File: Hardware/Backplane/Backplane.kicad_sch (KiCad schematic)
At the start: 9 parts, among them J1 10018784-10201TLF

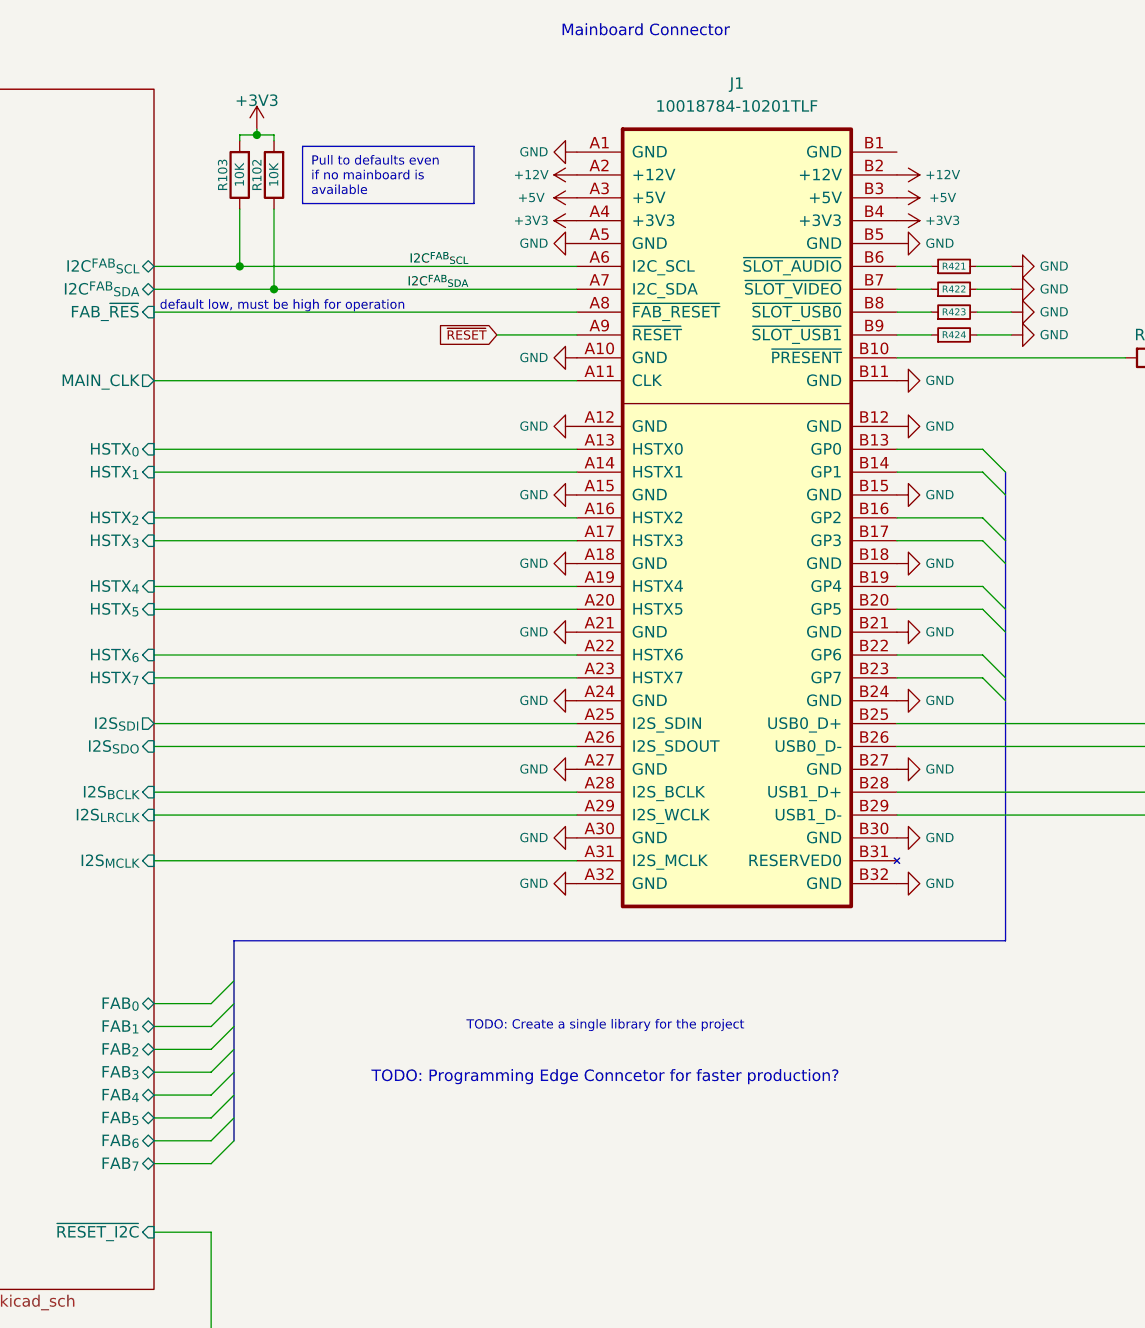
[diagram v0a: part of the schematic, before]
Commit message: Fixes several issues with the backplane schematic.
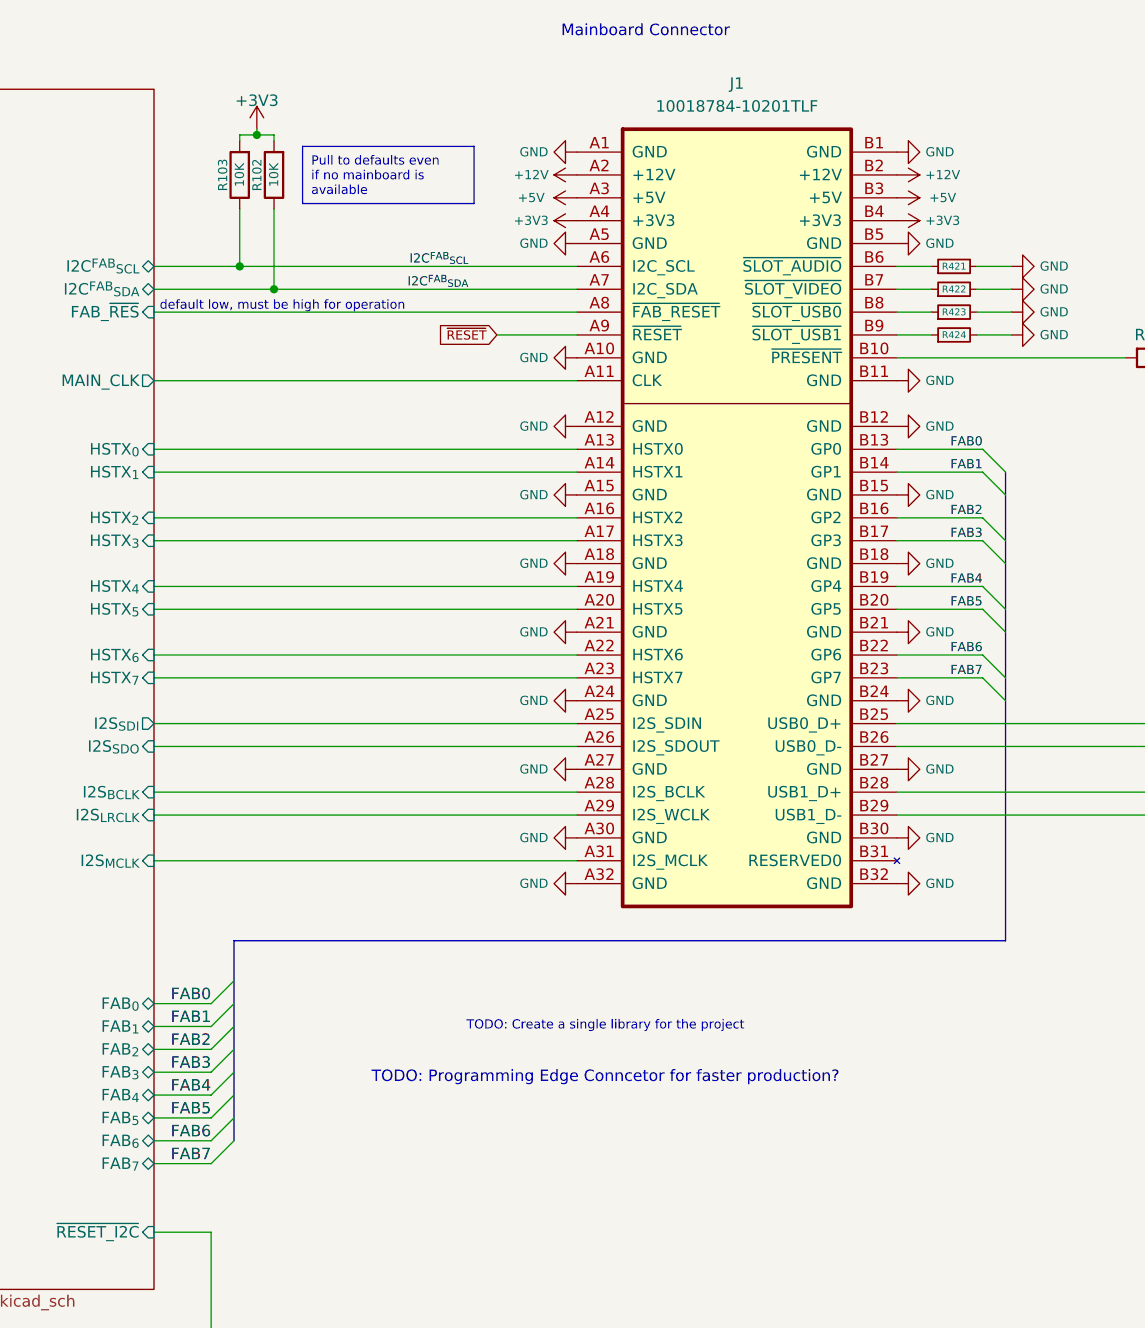
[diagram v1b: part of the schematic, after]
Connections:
- net GND: now also J1.B1 (GND)
- net FAB0: now reaches J1.B13 (GP0)
- net FAB1: now reaches J1.B14 (GP1)
- net FAB2: now reaches J1.B16 (GP2)
- net FAB3: now reaches J1.B17 (GP3)
- net FAB4: now reaches J1.B19 (GP4)
- net FAB5: now reaches J1.B20 (GP5)
- net FAB6: now reaches J1.B22 (GP6)
- net FAB7: now reaches J1.B23 (GP7)
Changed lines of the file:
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@@
+		)
+	)
+	(label "FAB4"
+		(at 82.55 137.16 180)
+		(effects
+			(font
+				(size 1.27 1.27)
+			)
+			(justify right bottom)
+		)
+	)
+	(label "FAB3"
+		(at 82.55 134.62 180)
+		(effects
+			(font
+				(size 1.27 1.27)
+			)
+			(justify right bottom)
 		)
 	)
@@
 		)
 	)
+	(label "FAB5"
+		(at 168.275 83.185 180)
+		(effects
+			(font
+				(size 1.016 1.016)
+			)
+			(justify right bottom)
+		)
+	)
+	(label "FAB1"
+		(at 168.275 67.945 180)
+		(effects
+			(font
+				(size 1.016 1.016)
+			)
+			(justify right bottom)
+		)
+	)
 	(label "USB_{1}_D+"
 		(at 221.615 111.76 0)
@@
 		)
 	)
+	(label "FAB3"
+		(at 168.275 75.565 180)
+		(effects
+			(font
+				(size 1.016 1.016)
+			)
+			(justify right bottom)
+		)
+	)
+	(label "FAB7"
+		(at 168.275 90.805 180)
+		(effects
+			(font
+				(size 1.016 1.016)
+			)
+			(justify right bottom)
+		)
+	)
+	(label "FAB0"
+		(at 168.275 65.405 180)
+		(effects
+			(font
+				(size 1.016 1.016)
+			)
+			(justify right bottom)
+		)
+	)
+	(label "FAB5"
+		(at 82.55 139.7 180)
+		(effects
+			(font
+				(size 1.27 1.27)
+			)
+			(justify right bottom)
+		)
+	)
+	(label "FAB2"
+		(at 82.55 132.08 180)
+		(effects
+			(font
+				(size 1.27 1.27)
+			)
+			(justify right bottom)
+		)
+	)
+	(label "FAB6"
+		(at 168.275 88.265 180)
+		(effects
+			(font
+				(size 1.016 1.016)
+			)
+			(justify right bottom)
+		)
+	)
+	(label "FAB0"
+		(at 82.55 127 180)
+		(effects
+			(font
+				(size 1.27 1.27)
+			)
+			(justify right bottom)
+		)
+	)
+	(label "FAB1"
+		(at 82.55 129.54 180)
+		(effects
+			(font
+				(size 1.27 1.27)
+			)
+			(justify right bottom)
+		)
+	)
+	(label "FAB2"
+		(at 168.275 73.025 180)
+		(effects
+			(font
+				(size 1.016 1.016)
+			)
+			(justify right bottom)
+		)
+	)
 	(label "USB_{0}_D-"
 		(at 221.615 98.425 0)
@@
 			)
 			(justify left bottom)
+		)
+	)
+	(label "FAB6"
+		(at 82.55 142.24 180)
+		(effects
+			(font
+				(size 1.27 1.27)
+			)
+			(justify right bottom)
+		)
+	)
+	(label "FAB4"
+		(at 168.275 80.645 180)
+		(effects
+			(font
+				(size 1.016 1.016)
+			)
+			(justify right bottom)
+		)
+	)
+	(label "FAB7"
+		(at 82.55 144.78 180)
+		(effects
+			(font
+				(size 1.27 1.27)
+			)
+			(justify right bottom)
 		)
 	)
@@
 					(unit 1)
 				)
+			)
+		)
+	)
+	(symbol
+		(lib_id "power:GND")
+		(at 158.75 32.385 90)
+		(mirror x)
+		(unit 1)
+		(body_style 1)
+		(exclude_from_sim no)
+		(in_bom yes)
+		(on_board yes)
+		(in_pos_files yes)
+		(dnp no)
+		(property "Reference" "#PWR01036"
+			(at 165.1 32.385 0)
+			(hide yes)
+			(show_name no)
+			(do_not_autoplace no)
+			(effects
+				(font
+					(size 1.016 1.016)
+				)
+			)
+		)
+		(property "Value" "GND"
+			(at 161.925 32.385 90)
+			(show_name no)
+			(do_not_autoplace no)
+			(effects
+				(font
+					(size 1.016 1.016)
+				)
+				(justify right)
+			)
+		)
+		(property "Footprint" ""
+			(at 158.75 32.385 0)
+			(hide yes)
+			(show_name no)
+			(do_not_autoplace no)
+			(effects
+				(font
+					(size 1.27 1.27)
+				)
+			)
+		)
+		(property "Datasheet" ""
+			(at 158.75 32.385 0)
+			(hide yes)
+			(show_name no)
+			(do_not_autoplace no)
+			(effects
+				(font
+					(size 1.27 1.27)
+				)
+			)
+		)
+		(property "Description" "Power symbol creates a global label with name \"GND\" , ground"
+			(at 158.75 32.385 0)
+			(hide yes)
+			(show_name no)
+			(do_not_autoplace no)
+			(effects
+				(font
+					(size 1.27 1.27)
+				)
+			)
+		)
+		(pin "1"
+		)
+		(instances
+			(project "Backplane"
+				(path "/c6da991a-d3ed-4ac1-8b0d-12cd7ba8539b"
+					(reference "#PWR01036")
+					(unit 1)
+				)

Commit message: Improves backplane schematic even more
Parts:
- added R441: 0, Resistor_SMD:R_0603_1608Metric, symbol Device:R_Small
- J1: symbol Home Computer:AHC-CONN-CPU -> Home Computer:AHC-CONN-CPU-HOST
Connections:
- net +3V3: now also R441.1
- net GND: no longer J1.A5 (GND)
- new net: J1.A5 (+3V3_ID), R441.2
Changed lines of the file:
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@@
 		(color 0 0 0 0)
 	)
+	(junction
+		(at 114.3 42.545)
+		(diameter 0)
+		(color 0 0 0 0)
+	)
 	(bus_entry
 		(at 82.55 137.16)
@@
 	(wire
 		(pts
+			(xy 113.665 42.545) (xy 114.3 42.545)
+		)
+		(stroke
+			(width 0)
+			(type default)
+		)
+	)
+	(wire
+		(pts
 			(xy 76.2 142.24) (xy 82.55 142.24)
 		)
@@
 	(wire
 		(pts
+			(xy 107.95 42.545) (xy 108.585 42.545)
+		)
+		(stroke
+			(width 0)
+			(type default)
+		)
+	)
+	(wire
+		(pts
 			(xy 76.2 152.4) (xy 82.55 152.4)
 		)
@@
 	(wire
 		(pts
+			(xy 114.3 42.545) (xy 123.19 42.545)
+		)
+		(stroke
+			(width 0)
+			(type default)
+		)
+	)
+	(wire
+		(pts
 			(xy 76.2 50.165) (xy 123.19 50.165)
 		)
@@
 	)
 	(symbol
-		(lib_id "Home Computer:AHC-CONN-CPU")
+		(lib_id "Home Computer:AHC-CONN-CPU-HOST")
 		(at 140.97 73.025 0)
 		(unit 1)
@@
 	)
 	(symbol
+		(lib_id "power:PWR_FLAG")
+		(at 114.3 42.545 0)
+		(unit 1)
+		(body_style 1)
+		(exclude_from_sim no)
+		(in_bom yes)
+		(on_board yes)
+		(in_pos_files yes)
+		(dnp no)
+		(fields_autoplaced yes)
+		(property "Reference" "#FLG0439"
+			(at 114.3 40.64 0)
+			(hide yes)
+			(show_name no)
+			(do_not_autoplace no)
+			(effects
+				(font
+					(size 1.016 1.016)
+				)
+			)
+		)
+		(property "Value" "PWR_FLAG"
+			(at 114.3 37.465 0)
+			(hide yes)
+			(show_name no)
+			(do_not_autoplace no)
+			(effects
+				(font
+					(size 1.016 1.016)
+				)
+			)
+		)
+		(property "Footprint" ""
+			(at 114.3 42.545 0)
+			(hide yes)
+			(show_name no)
+			(do_not_autoplace no)
+			(effects
+				(font
+					(size 1.27 1.27)
+				)
+			)
+		)
+		(property "Datasheet" ""
+			(at 114.3 42.545 0)
+			(hide yes)
+			(show_name no)
+			(do_not_autoplace no)
+			(effects
+				(font
+					(size 1.27 1.27)
+				)
+			)
+		)
+		(property "Description" "Special symbol for telling ERC where power comes from"
+			(at 114.3 42.545 0)
+			(hide yes)
+			(show_name no)
+			(do_not_autoplace no)
+			(effects
+				(font
+					(size 1.27 1.27)
+				)
+			)
+		)
+		(pin "1"
+		)
+		(instances
+			(project "Backplane"
+				(path "/c6da991a-d3ed-4ac1-8b0d-12cd7ba8539b"
+					(reference "#FLG0439")
+					(unit 1)
+				)
+			)
+		)
+	)
+	(symbol
 		(lib_id "power:GND")
 		(at 123.19 100.965 270)
@@
 	)
 	(symbol
+		(lib_id "power:+3V3")
+		(at 107.95 42.545 90)
+		(mirror x)
+		(unit 1)
+		(body_style 1)
+		(exclude_from_sim no)
+		(in_bom yes)
+		(on_board yes)
+		(in_pos_files yes)
+		(dnp no)
+		(property "Reference" "#PWR0133"
+			(at 111.76 42.545 0)
+			(hide yes)
+			(show_name no)
+			(do_not_autoplace no)
+			(effects
+				(font
+					(size 1.016 1.016)
+				)
+			)
+		)
+		(property "Value" "+3V3"
+			(at 102.87 42.545 90)
+			(show_name no)
+			(do_not_autoplace no)
+			(effects
+				(font
+					(size 1.016 1.016)
+				)
+			)
+		)
+		(property "Footprint" ""
+			(at 107.95 42.545 0)
+			(hide yes)
+			(show_name no)
+			(do_not_autoplace no)
+			(effects
+				(font
+					(size 1.27 1.27)
+				)
+			)
+		)
+		(property "Datasheet" ""
+			(at 107.95 42.545 0)
+			(hide yes)
+			(show_name no)
+			(do_not_autoplace no)
+			(effects
+				(font
+					(size 1.27 1.27)
+				)
+			)
+		)
+		(property "Description" "Power symbol creates a global label with name \"+3V3\""
+			(at 107.95 42.545 0)
+			(hide yes)
+			(show_name no)
+			(do_not_autoplace no)
+			(effects
+				(font
+					(size 1.27 1.27)
+				)
+			)
+		)
+		(pin "1"
+		)
+		(instances
+			(project "Backplane"
+				(path "/c6da991a-d3ed-4ac1-8b0d-12cd7ba8539b"
+					(reference "#PWR0133")
+					(unit 1)
+				)
+			)
+		)
+	)
+	(symbol
+		(lib_id "Device:R_Small")
+		(at 111.125 42.545 90)
+		(unit 1)
+		(body_style 1)
+		(exclude_from_sim no)
+		(in_bom yes)
+		(on_board yes)
+		(in_pos_files yes)
+		(dnp no)
+		(property "Reference" "R441"
+			(at 111.125 42.545 90)
+			(show_name no)
+			(do_not_autoplace no)
+			(effects
+				(font
+					(size 0.762 0.762)
+				)
+			)
+		)
+		(property "Value" "0"
+			(at 111.125 40.005 90)
+			(hide yes)
+			(show_name no)
+			(do_not_autoplace no)
+			(effects
+				(font
+					(size 1.016 1.016)
+				)
+			)
+		)
+		(property "Footprint" "Resistor_SMD:R_0603_1608Metric"
+			(at 111.125 42.545 0)
+			(hide yes)
+			(show_name no)
+			(do_not_autoplace no)
+			(effects
+				(font
+					(size 1.27 1.27)
+				)
+			)
+		)
+		(property "Datasheet" "https://www.yageogroup.com/content/datasheet/asset/file/PYU-RC_GROUP_51_ROHS_L"
+			(at 111.125 42.545 0)
+			(hide yes)
+			(show_name no)
+			(do_not_autoplace no)
+			(effects
+				(font
+					(size 1.27 1.27)
+				)
+			)
+		)
+		(property "Description" "Resistor, small symbol"
+			(at 111.125 42.545 0)
+			(hide yes)
+			(show_name no)
+			(do_not_autoplace no)
+			(effects
+				(font
+					(size 1.27 1.27)
+				)
+			)
+		)
+		(property "Digikey Part No" "311-0.0GRCT-ND"
+			(at 111.125 42.545 90)
+			(hide yes)
+			(show_name no)
+			(do_not_autoplace no)
+			(effects
+				(font
+					(size 1.27 1.27)
+				)
+			)
+		)
+		(pin "2"
+		)
+		(pin "1"
+		)
+		(instances
+			(project "Backplane"
+				(path "/c6da991a-d3ed-4ac1-8b0d-12cd7ba8539b"
+					(reference "R441")
+					(unit 1)
+				)
+			)
+		)
+	)
+	(symbol
 		(lib_id "power:GND")
 		(at 158.75 78.105 90)
@@
 					(unit 1)
 				)
-			)
-		)
-	)
-	(symbol
-		(lib_id "power:GND")
-		(at 123.19 42.545 270)
-		(unit 1)
-		(body_style 1)
-		(exclude_from_sim no)
-		(in_bom yes)
-		(on_board yes)
-		(in_pos_files yes)
-		(dnp no)
-		(property "Reference" "#PWR01014"
-			(at 116.84 42.545 0)
-			(hide yes)
-			(show_name no)
-			(do_not_autoplace no)
-			(effects
-				(font
-					(size 1.016 1.016)
-				)
-			)
-		)
-		(property "Value" "GND"
-			(at 120.015 42.545 90)
-			(show_name no)
-			(do_not_autoplace no)
-			(effects
-				(font
-					(size 1.016 1.016)
-				)
-				(justify right)
-			)
-		)
-		(property "Footprint" ""
-			(at 123.19 42.545 0)
-			(hide yes)
-			(show_name no)
-			(do_not_autoplace no)
-			(effects
-				(font
-					(size 1.27 1.27)
-				)
-			)
-		)
-		(property "Datasheet" ""
-			(at 123.19 42.545 0)
-			(hide yes)
-			(show_name no)
-			(do_not_autoplace no)
-			(effects
-				(font
-					(size 1.27 1.27)
-				)
-			)
-		)
-		(property "Description" "Power symbol creates a global label with name \"GND\" , ground"
-			(at 123.19 42.545 0)
-			(hide yes)
-			(show_name no)
-			(do_not_autoplace no)
-			(effects
-				(font
-					(size 1.27 1.27)
-				)
-			)
-		)
-		(pin "1"
-		)
-		(instances
-			(project "Backplane"
-				(path "/c6da991a-d3ed-4ac1-8b0d-12cd7ba8539b"
-					(reference "#PWR01014")
-					(unit 1)
-				)
